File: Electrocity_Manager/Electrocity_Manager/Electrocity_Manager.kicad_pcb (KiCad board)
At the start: 2 copper layers, 100 x 77 mm, 190 parts, among them IC2 MAIN_SHUTDOWN, IC3 RELAY_STATE, IC4 ADC_RST, J1 SERIAL, P1 SWD, P10 EMERGENCY, P11 EMERGENCY, P12 FRAME_GRAND, P13 BATT_IN, P14 POWER_OUT, P15 FUN_OUT, P16 BATT_IN, P17 POWER_OUT, P18 FUN_OUT, P2 CAN, P3 CAN, P4 EMERGENCY_SIGNAL, P5 EMERGENCY_SIGNAL, P6 12V_OUT, P7 12V_OUT, P9 MAIN_SW, Q1 FET_N, Q2 NPN, Q3 NPN, Q7 FET_N, SW1 RST, SW2 SW0, SW3 SW1, U1 MAX3051, U10 BD9G101G, U11 ACS781, U12 V23134J1052D642, U13 ACS70331, U14 ACS781, U15 BD33FA1, U16 LOGO, U17 LOGO, U18 LOGO, U19 MCP2221A, U2 STM32F405RG, U20 OSRB38C9AA, U21 OSRB38C9AA, U22 HSIN_946, U23 LOGO, U24 LOGO, U25 LOGO, U26 LOGO, U3 FULL COLOR, U4 AQM0802_BL, U5 AP3211, U6 SI8900, U7 AZ1086H, U8 V23134J1052D642, U9 RPA60-12FW/N, X1 8MHz

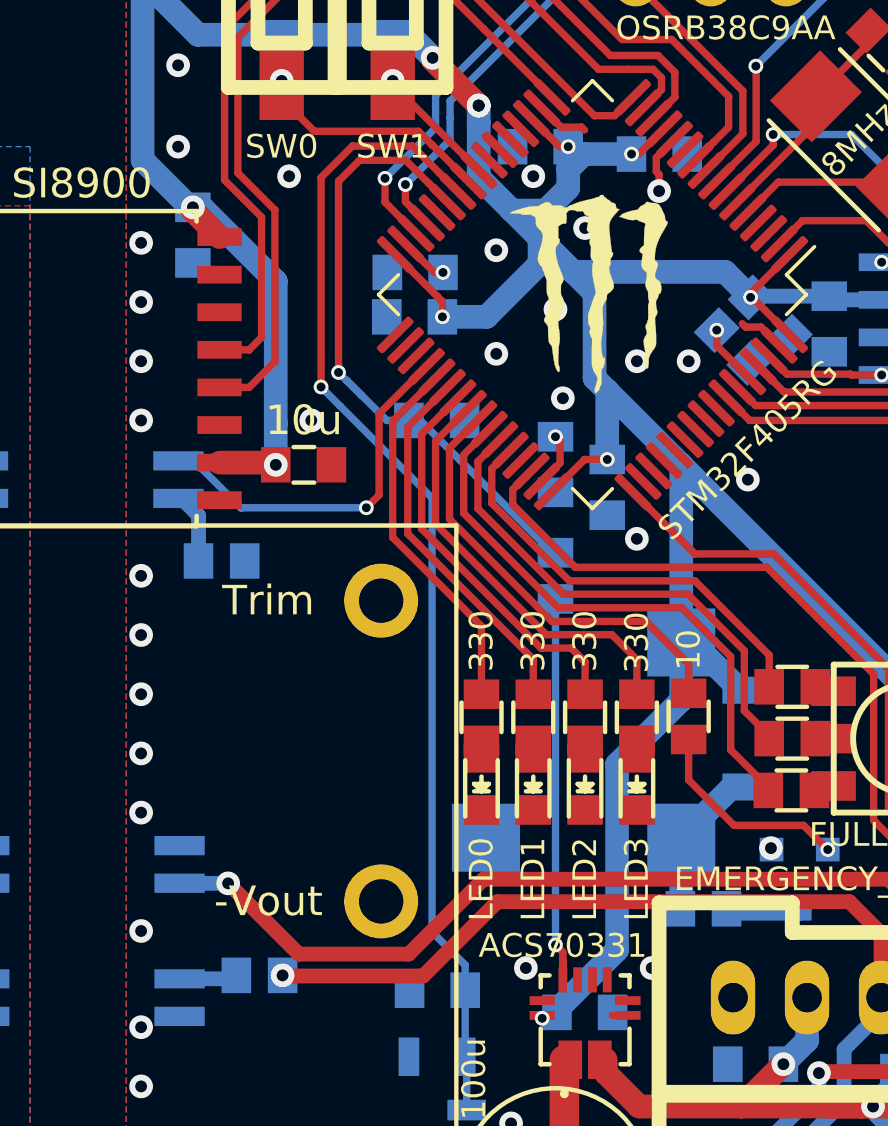
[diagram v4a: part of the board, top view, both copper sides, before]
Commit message: ピカチュウたちの配線を変えた。
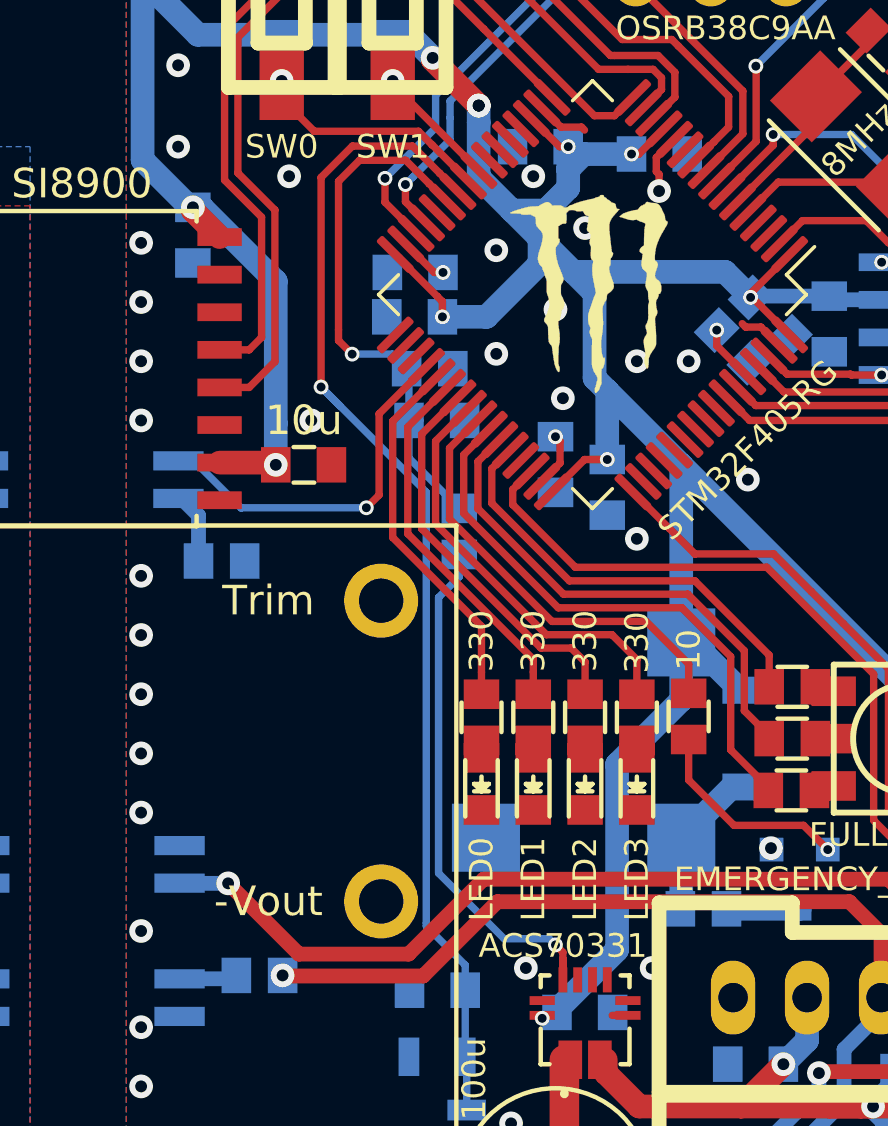
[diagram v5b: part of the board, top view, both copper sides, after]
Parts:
- added R43: 10k, Mizz_lib:R_0603, B.Cu at (119.8, 144.0)
- moved R47 3.58 mm to (120.8, 149.5)
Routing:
- net Net-(R47-Pad2): track 13.8 -> 18.0 mm
- net /ADC12_IN9: track 21.6 -> 18.5 mm
- net /ADC12_IN8: track 39.3 -> 40.3 mm
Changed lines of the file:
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@@
     (thickness 1.6)
     (drawings 37)
-    (tracks 1359)
+    (tracks 1366)
     (zones 0)
-    (modules 190)
+    (modules 191)
     (nets 157)
   )
@@
   )
   (setup
-    (last_trace_width 0.8)
+    (last_trace_width 0.25)
     (user_trace_width 0.3)
     (user_trace_width 0.5)
@@
       (effects (font (size 1 1) (thickness 0.15)) (justify mirror))
     )
-    (fp_text value 1u (at 0 -1.25) (layer B.SilkS)
+    (fp_text value 1u (at 2.25 0) (layer B.SilkS)
       (effects (font (size 0.8 0.8) (thickness 0.15)) (justify mirror))
     )
@@
   )
   (module Mizz_lib:R_0603 (layer B.Cu)
-    (at 124 151 270)
+    (at 120.75 149.5 270)
     (descr "Resistor SMD 0603, reflow soldering, Vishay (see dcrcw.pdf)")
     (tags "resistor 0603")
@@
       (xy -2.971518 1.553268)) (layer B.SilkS) (width 0.01))
   )
+  (module Mizz_lib:R_0603 (layer B.Cu)
+    (at 119.75 144)
+    (descr "Resistor SMD 0603, reflow soldering, Vishay (see dcrcw.pdf)")
+    (tags "resistor 0603")
+    (attr smd)
+    (fp_text reference R43 (at 0 1.9) (layer B.SilkS) hide
+      (effects (font (size 1 1) (thickness 0.15)) (justify mirror))
+    )
+    (fp_text value 10k (at 2.5 0) (layer B.SilkS)
+      (effects (font (size 0.8 0.8) (thickness 0.15)) (justify mirror))
+    )
+    (fp_line (start -1.3 0.8) (end 1.3 0.8) (layer B.CrtYd) (width 0.05))
+    (fp_line (start -1.3 -0.8) (end 1.3 -0.8) (layer B.CrtYd) (width 0.05))
+    (fp_line (start -1.3 0.8) (end -1.3 -0.8) (layer B.CrtYd) (width 0.05))
+    (fp_line (start 1.3 0.8) (end 1.3 -0.8) (layer B.CrtYd) (width 0.05))
+    (fp_line (start 0.5 -0.675) (end -0.5 -0.675) (layer B.SilkS) (width 0.15))
+    (fp_line (start -0.5 0.675) (end 0.5 0.675) (layer B.SilkS) (width 0.15))
+    (pad 1 smd rect (at -0.78 0) (size 1 1.2) (layers B.Cu B.Paste B.Mask)
+      (net 153 /ADC12_IN9))
+    (pad 2 smd rect (at 0.78 0) (size 1 1.2) (layers B.Cu B.Paste B.Mask)
+      (net 1 GND))
+    (model C:/Users/Mizuta/Downloads/kicad-packages3D-master/Resistor_SMD.3dshapes/R_0603_1608Metric.step
+      (at (xyz 0 0 0))
+      (scale (xyz 1 1 1))
+      (rotate (xyz 0 0 0))
+    )
+  )
   (gr_text "Pocket Monster \n\"Pikachu\"" (at 93 146.75) (layer B.SilkS)
     (effects (font (size 2 2) (thickness 0.5) italic) (justify left mirror))
@@
   (segment (start 124.25 163.72) (end 124 163.47) (width 0.25) (layer F.Cu) (net 84))
   (segment (start 124.25 164.65) (end 124.25 163.72) (width 0.25) (layer F.Cu) (net 84))
-  (segment (start 124 155.78) (end 124 163.47) (width 0.25) (layer B.Cu) (net 84))
-  (segment (start 124 152.3) (end 123.95 152.25) (width 0.25) (layer B.Cu) (net 84))
-  (segment (start 124 155.78) (end 124 151.78) (width 0.25) (layer B.Cu) (net 84))
+  (segment (start 124 163.47) (end 123.79 163.26) (width 0.25) (layer B.Cu) (net 84))
+  (segment (start 122.264998 163.26) (end 120.05 161.045002) (width 0.25) (layer B.Cu) (net 84))
+  (segment (start 123.79 163.26) (end 122.264998 163.26) (width 0.25) (layer B.Cu) (net 84))
+  (segment (start 120.75 151.03) (end 120.75 150.28) (width 0.25) (layer B.Cu) (net 84))
+  (segment (start 120.05 151.73) (end 120.75 151.03) (width 0.25) (layer B.Cu) (net 84))
+  (segment (start 120.05 161.045002) (end 120.05 151.73) (width 0.25) (layer B.Cu) (net 84))
   (via (at 135.02 144.215) (size 0.5) (drill 0.3) (layers F.Cu B.Cu) (net 85))
   (segment (start 131.826093 144.187005) (end 131.207375 143.568287) (width 0.25) (layer F.Cu) (net 85))
@@
   (segment (start 126.75 153.83) (end 126.75 155) (width 0.25) (layer F.Cu) (net 152))
   (segment (start 125.91 152.99) (end 126.75 153.83) (width 0.25) (layer F.Cu) (net 152))
-  (segment (start 117.46 144.91) (end 117.45 144.91) (width 0.25) (layer B.Cu) (net 153))
   (segment (start 119.734568 137.752334) (end 119.732334 137.752334) (width 0.25) (layer F.Cu) (net 153))
   (segment (start 120.353286 138.371052) (end 119.734568 137.752334) (width 0.25) (layer F.Cu) (net 153))
   (segment (start 119.732334 137.752334) (end 118.94 136.96) (width 0.25) (layer F.Cu) (net 153))
   (segment (start 118.94 136.96) (end 117.38 136.96) (width 0.25) (layer F.Cu) (net 153))
-  (via (at 116.67 144.13) (size 0.5) (drill 0.3) (layers F.Cu B.Cu) (net 153))
   (segment (start 117.38 136.96) (end 116.67 137.67) (width 0.25) (layer F.Cu) (net 153))
-  (segment (start 116.67 137.67) (end 116.67 144.13) (width 0.25) (layer F.Cu) (net 153))
-  (segment (start 117.46 144.91) (end 116.95 144.4) (width 0.25) (layer B.Cu) (net 153))
-  (segment (start 116.67 144.13) (end 116.94 144.4) (width 0.25) (layer B.Cu) (net 153))
   (segment (start 119.43 145.75) (end 119.05 145.75) (width 0.25) (layer B.Cu) (net 153))
-  (segment (start 123.9 150.22) (end 119.43 145.75) (width 0.25) (layer B.Cu) (net 153))
-  (segment (start 124 150.22) (end 123.9 150.22) (width 0.25) (layer B.Cu) (net 153))
-  (segment (start 116.95 144.4) (end 116.94 144.4) (width 0.25) (layer B.Cu) (net 153))
-  (segment (start 118.3 145.75) (end 116.95 144.4) (width 0.25) (layer B.Cu) (net 153))
-  (segment (start 119.05 145.75) (end 118.3 145.75) (width 0.25) (layer B.Cu) (net 153))
+  (segment (start 119.05 145.75) (end 119.05 144.08) (width 0.25) (layer B.Cu) (net 153) (status C00000))
+  (segment (start 119.05 144.08) (end 118.97 144) (width 0.25) (layer B.Cu) (net 153) (status C00000))
+  (segment (start 118.97 144) (end 118.97 143.99) (width 0.25) (layer B.Cu) (net 153))
+  (via (at 117.13 143.51) (size 0.5) (drill 0.3) (layers F.Cu B.Cu) (net 153))
+  (segment (start 118.97 143.99) (end 118.49 143.51) (width 0.25) (layer B.Cu) (net 153))
+  (segment (start 118.49 143.51) (end 117.13 143.51) (width 0.25) (layer B.Cu) (net 153))
+  (segment (start 116.67 143.05) (end 116.67 142.69) (width 0.25) (layer F.Cu) (net 153))
+  (segment (start 117.13 143.51) (end 116.67 143.05) (width 0.25) (layer F.Cu) (net 153))
+  (segment (start 116.67 137.67) (end 116.67 142.69) (width 0.25) (layer F.Cu) (net 153))
+  (segment (start 119.05 147.02) (end 120.75 148.72) (width 0.25) (layer B.Cu) (net 153))
+  (segment (start 119.05 145.75) (end 119.05 147.02) (width 0.25) (layer B.Cu) (net 153))
   (segment (start 121 167.3) (end 120.95 167.25) (width 0.25) (layer B.Cu) (net 154))
   (segment (start 121 169.05) (end 121 167.3) (width 0.25) (layer B.Cu) (net 154))
@@
   (segment (start 120.95 164.15) (end 119.83 163.03) (width 0.25) (layer B.Cu) (net 154))
   (segment (start 120.95 165) (end 120.95 164.15) (width 0.25) (layer B.Cu) (net 154))
-  (segment (start 119.83 163.03) (end 119.83 148.37) (width 0.25) (layer B.Cu) (net 154))
-  (segment (start 119.83 148.37) (end 116.72 145.26) (width 0.25) (layer B.Cu) (net 154))
-  (segment (start 120.088121 137.398781) (end 120.088121 137.398121) (width 0.25) (layer F.Cu) (net 154))
-  (segment (start 120.706839 138.017499) (end 120.088121 137.398781) (width 0.25) (layer F.Cu) (net 154))
-  (segment (start 120.088121 137.398121) (end 119.17 136.48) (width 0.25) (layer F.Cu) (net 154))
+  (segment (start 119.83 163.03) (end 119.66 162.86) (width 0.25) (layer B.Cu) (net 154))
+  (segment (start 119.635001 162.835001) (end 119.635001 162.732001) (width 0.25) (layer B.Cu) (net 154))
+  (segment (start 119.66 162.86) (end 119.635001 162.835001) (width 0.25) (layer B.Cu) (net 154))
+  (segment (start 119.635001 148.175001) (end 115.99 144.53) (width 0.25) (layer B.Cu) (net 154))
+  (segment (start 119.635001 162.732001) (end 119.635001 148.175001) (width 0.25) (layer B.Cu) (net 154))
   (segment (start 116.72 145.26) (end 116.23 144.77) (width 0.25) (layer B.Cu) (net 154))
-  (via (at 116.08 144.62) (size 0.5) (drill 0.3) (layers F.Cu B.Cu) (net 154))
-  (segment (start 116.23 144.77) (end 116.08 144.62) (width 0.25) (layer B.Cu) (net 154))
   (segment (start 116.08 137.54) (end 117.14 136.48) (width 0.25) (layer F.Cu) (net 154))
-  (segment (start 116.08 144.62) (end 116.08 137.54) (width 0.25) (layer F.Cu) (net 154))
   (segment (start 119.17 136.48) (end 117.14 136.48) (width 0.25) (layer F.Cu) (net 154))
+  (segment (start 116.08 144.62) (end 116.08 137.54) (width 0.25) (layer F.Cu) (net 154))
+  (segment (start 116.23 144.77) (end 116.08 144.62) (width 0.25) (layer B.Cu) (net 154))
+  (segment (start 120.088121 137.398121) (end 119.17 136.48) (width 0.25) (layer F.Cu) (net 154))
+  (segment (start 120.706839 138.017499) (end 120.088121 137.398781) (width 0.25) (layer F.Cu) (net 154))
+  (segment (start 120.088121 137.398781) (end 120.088121 137.398121) (width 0.25) (layer F.Cu) (net 154))
+  (via (at 116.08 144.62) (size 0.5) (drill 0.3) (layers F.Cu B.Cu) (net 154))
   (segment (start 81.55048 162.44996) (end 83.08004 162.44996) (width 0.8) (layer B.Cu) (net 156))
   (segment (start 83.25 162.47) (end 83.25 161.03) (width 1) (layer B.Cu) (net 156))
@@
       )
     )
+  )
+  (zone (net 0) (net_name "") (layer B.Cu) (hatch edge 0.508)
+    (connect_pads (clearance 0.3))
+    (min_thickness 0.254)
+    (keepout (tracks allowed) (vias allowed) (copperpour not_allowed))
+    (fill (arc_segments 16) (thermal_gap 0.508) (thermal_bridge_width 0.508))
+    (polygon
+      (pts
+        (xy 121 152.75) (xy 128.75 152.75) (xy 128.75 160.5) (xy 121 160.5)
+      )
+    )
